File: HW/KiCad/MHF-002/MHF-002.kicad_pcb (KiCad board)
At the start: 2 copper layers, 99.9 x 99.9 mm, 264 parts, among them J1 VGA, J10 I2C, J100 x, J101 x, J102 x, J103 x, J104 x, J105 x, J106 x, J107 +3V3, J108 GND, J109 +3V3, J11 + 5V -, J110 +5V, J111 GND, J112 GND, J12 Reset, J13 +5V, J14 GND, J15 AREF, J16 XTAL2, J17 SDcard, J18 XTAL1, J19 AVCC, J2 PS/2, J20 SDcardpins, J21 x, J22 x, J23 VIN 12V, J24 AND_B1, J25 AND_B2, J26 AND_C1, J27 AND_C2, J28 AND_D1, J29 AND_D2, J3 RCA, J30 AND_Dx, J31 AND_Cx, J32 AND_Bx, J33 NOTF, J34 NOTE, J35 NOTEx, J36 NOTFx, J37 x, J38 x, J39 x, J4 SysBus, J40 x, J41 x, J42 x, J43 x, J44 x, J45 x, J46 x, J47 x, J48 x, J49 x, J5 Micro, J50 x, J51 x, J52 x, J53 x, J54 x, J55 x, J56 x, J57 x, J58 x, J59 x, J6 SysBus, J60 x, J61 x, J62 x, J63 x, J64 x, J65 x, J66 x, J67 x, J68 x, J69 x, J7 SPI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

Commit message: photos and tests
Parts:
- U14: value 5.0V -> AMS1117-5.0
- U15: value 3.3 V -> AMS1117-3.3
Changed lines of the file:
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@@
 		)
 		(property "Value" "+ 5V -"
-			(at -1.23661 -2.7672 0)
+			(at -1.23661 -2.7672 180)
 			(unlocked yes)
 			(layer "F.SilkS")
@@
 			)
 		)
-		(property "Value" "3.3 V"
+		(property "Value" "AMS1117-3.3"
 			(at 5.62716 -1.77458 270)
 			(unlocked yes)
@@
 			)
 		)
-		(property "Value" "5.0V"
+		(property "Value" "AMS1117-5.0"
 			(at 4.55012 -2.31835 90)
 			(unlocked yes)

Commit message: external memory
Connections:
- net Net-(M3-A0) renamed /L3
- net Net-(M3-A1) renamed /L2
- net Net-(M3-A2) renamed /L1
- net Net-(M3-A3) renamed /L0
- net Net-(M3-A4) renamed /L4
- net Net-(M3-A5) renamed /L5
- net Net-(M3-A6) renamed /L6
- net Net-(M3-A7) renamed /L7

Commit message: +footprints
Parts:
- removed U4: 74HC165, Package_DIP:DIP-16_W7.62mm
- added JP15: TX340, Jumper:SolderJumper-2_P1.3mm_Open_RoundedPad1.0x1.5mm, F.Cu at (-18.3, 35.7)
- added JP16: RX340, Jumper:SolderJumper-2_P1.3mm_Open_RoundedPad1.0x1.5mm, F.Cu at (-18.3, 39.2)
- added JP17: CTS340, Jumper:SolderJumper-2_P1.3mm_Open_RoundedPad1.0x1.5mm, F.Cu at (-18.3, 42.8)
- added JP18: DTR340, Jumper:SolderJumper-2_P1.3mm_Open_RoundedPad1.0x1.5mm, F.Cu at (-18.3, 46.3)
- added JP19: RTS340, Jumper:SolderJumper-2_P1.3mm_Open_RoundedPad1.0x1.5mm, F.Cu at (-18.3, 49.9)
- added JP20: USB_GND, MHF:G_rework_jumper_2.54mm, F.Cu at (94.5, 40.6)
- added M1: CP2102, MHF:G_CP2102, F.Cu at (223.5, 106.7)
- added R44: 10k, Resistor_SMD:R_0805_2012Metric_Pad1.20x1.40mm_HandSolder, F.Cu at (-3.26, 51.7)
- added R45: 10k, Resistor_SMD:R_0805_2012Metric_Pad1.20x1.40mm_HandSolder, F.Cu at (-3.26, 54.7)
- added U5: 74HC166, MHF:G_SOIC-16_3.9x9.9mm_HandSolder, F.Cu at (230.2, 16.8)
- C9: footprint Capacitor_SMD:C_0603_1608Metric_Pad1.08x0.95mm_HandSolder -> Capacitor_THT:C_Disc_D3.0mm_W2.0mm_P2.50mm
- J2: footprint other.pretty:J_Mini-DIN-6 -> MHF:J_Mini-DIN-6
- J3: footprint Gilhad:CUI_RCJ-047_Yellow -> MHF:CUI_RCJ-047_Yellow
- M3, M5: footprint Package_SO:TSOP-I-32_18.4x8mm_P0.5mm -> MHF:G_TSOP-I-32_18.4x8mm_HandSolder
- U1: footprint Package_QFP:TQFP-100_14x14mm_P0.5mm -> MHF:G_TQFP-100_14x14mm_HandSolder
- U10, U11, U12: footprint Package_SO:SOIC-20W_7.5x12.8mm_P1.27mm -> MHF:G_SOIC-20W_7.5x12.8mm_P1.27mm_HandSolder
- moved Y1 136.3 mm to (216.1, 38.5), turned to 0 degrees
- moved M5 134.4 mm to (179.2, 53.3)
- moved C13 134.2 mm to (219.5, 42.4), turned to 180 degrees
- moved R29 133.5 mm to (216.0, 42.4), turned to 180 degrees
- moved C14 132.7 mm to (212.7, 42.4), turned to 0 degrees
- moved U1 129.5 mm to (214.2, 54.2), turned to 180 degrees
- moved J1 128.3 mm to (238.9, 95.2)
- moved J3 128.2 mm to (252.3, 54.9)
- moved H5 128.1 mm to (157.4, 30.4)
- moved H6 128.0 mm to (247.4, 30.4)
- moved H8 128.0 mm to (157.4, 120.4)
- moved H7 128.0 mm to (247.4, 120.4)
- moved J2 128.0 mm to (252.1, 72.4)
- moved J4 127.3 mm to (157.5, 36.1)
- moved J6 127.2 mm to (162.6, 36.1)
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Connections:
- C9 pad 2: Net-(U13-~{DTR}) -> Net-(JP18-B)
- J5 pad 5: GND -> Net-(J5-GND)
- J5 pad 6: GND -> Net-(J5-GND)
- JP55 pad 2: PS2 Data -> Net-(JP55-B)
- JP56 pad 2: PS2 Clock -> Net-(JP56-B)
- N1 pad 2: VGA data 4 -> VSyncVGA
- PB1 pad 5: PS2-OE -> CTS
- PB1 pad 6: X16 -> RTS
- PE1 pad 3: CTS -> PS2-OE
- PE1 pad 4: RTS -> X16
- PF1 pad 1: Shared_data_D0 -> VGA data 0
- PF1 pad 2: Shared_data_D1 -> VGA data 1
- PF1 pad 3: Shared_data_D2 -> VGA data 2
- PF1 pad 4: Shared_data_D3 -> VGA data 3
- PF1 pad 5: Shared_data_D4 -> VGA data 4
- PF1 pad 6: Shared_data_D5 -> VGA data 5
- PF1 pad 7: Shared_data_D6 -> VGA data 6
- PF1 pad 8: Shared_data_D7 -> VGA data 7
- PL1 pad 1: VGA data 0 -> Shared_data_D0
- PL1 pad 2: VGA data 1 -> Shared_data_D1
- PL1 pad 3: VGA data 2 -> Shared_data_D2
- PL1 pad 4: VGA data 3 -> Shared_data_D3
- PL1 pad 5: VGA data 4 -> Shared_data_D4
- PL1 pad 6: VGA data 5 -> Shared_data_D5
- PL1 pad 7: VGA data 6 -> Shared_data_D6
- PL1 pad 8: VGA data 7 -> Shared_data_D7
- R28 pad 2: Net-(U13-~{DTR}) -> Net-(JP18-B)
- U1 pad 23: PS2-OE -> CTS
- U1 pad 24: X16 -> RTS
- U1 pad 35: VGA data 0 -> Shared_data_D0
- U1 pad 36: VGA data 1 -> Shared_data_D1
- U1 pad 37: VGA data 2 -> Shared_data_D2
- U1 pad 38: VGA data 3 -> Shared_data_D3
- U1 pad 39: VGA data 4 -> Shared_data_D4
- U1 pad 4: CTS -> PS2-OE
- U1 pad 40: VGA data 5 -> Shared_data_D5
- U1 pad 41: VGA data 6 -> Shared_data_D6
- U1 pad 42: VGA data 7 -> Shared_data_D7
- U1 pad 5: RTS -> X16
- U1 pad 90: Shared_data_D7 -> VGA data 7
- U1 pad 91: Shared_data_D6 -> VGA data 6
- U1 pad 92: Shared_data_D5 -> VGA data 5
- U1 pad 93: Shared_data_D4 -> VGA data 4
- U1 pad 94: Shared_data_D3 -> VGA data 3
- U1 pad 95: Shared_data_D2 -> VGA data 2
- U1 pad 96: Shared_data_D1 -> VGA data 1
- U1 pad 97: Shared_data_D0 -> VGA data 0
- U13 pad 13: Net-(U13-~{DTR}) -> Net-(JP18-A)
- U13 pad 14: RTS -> Net-(JP19-A)
- U13 pad 2: M8TXD -> Net-(JP15-A)
- U13 pad 3: M8RXD -> Net-(JP16-A)
- U13 pad 9: CTS -> Net-(JP17-A)
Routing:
- net Shared_data_D1: track 149.9 -> 216.1 mm
- net VGA data 1: track 66.2 -> 0.00 mm
- net VGA data 6: track 57.8 -> 0.00 mm, vias 1 -> 0
- net Shared_data_D6: track 105.7 -> 163.5 mm, vias 2 -> 3
- net VGA data 2: track 55.5 -> 0.00 mm, vias 2 -> 0
- net Shared_data_D2: track 80.8 -> 136.3 mm, vias 1 -> 3
- net VGA data 7: track 55.5 -> 0.00 mm, vias 2 -> 0
- net Shared_data_D7: track 96.0 -> 151.5 mm, vias 1 -> 3
- net Shared_data_D0: track 76.2 -> 129.0 mm, vias 0 -> 1
- net VGA data 0: track 52.8 -> 0.00 mm, vias 1 -> 0
- net Shared_data_D5: track 102.4 -> 155.1 mm
- net VGA data 5: track 52.7 -> 0.00 mm
- net Net-(U13-~{DTR}): track 5.72 -> 0.00 mm, vias 1 -> 0
- net (no net): track 0.00 -> 5.72 mm, vias 0 -> 1
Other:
- board size 99.9 x 99.9 mm -> 228 x 101.2 mm

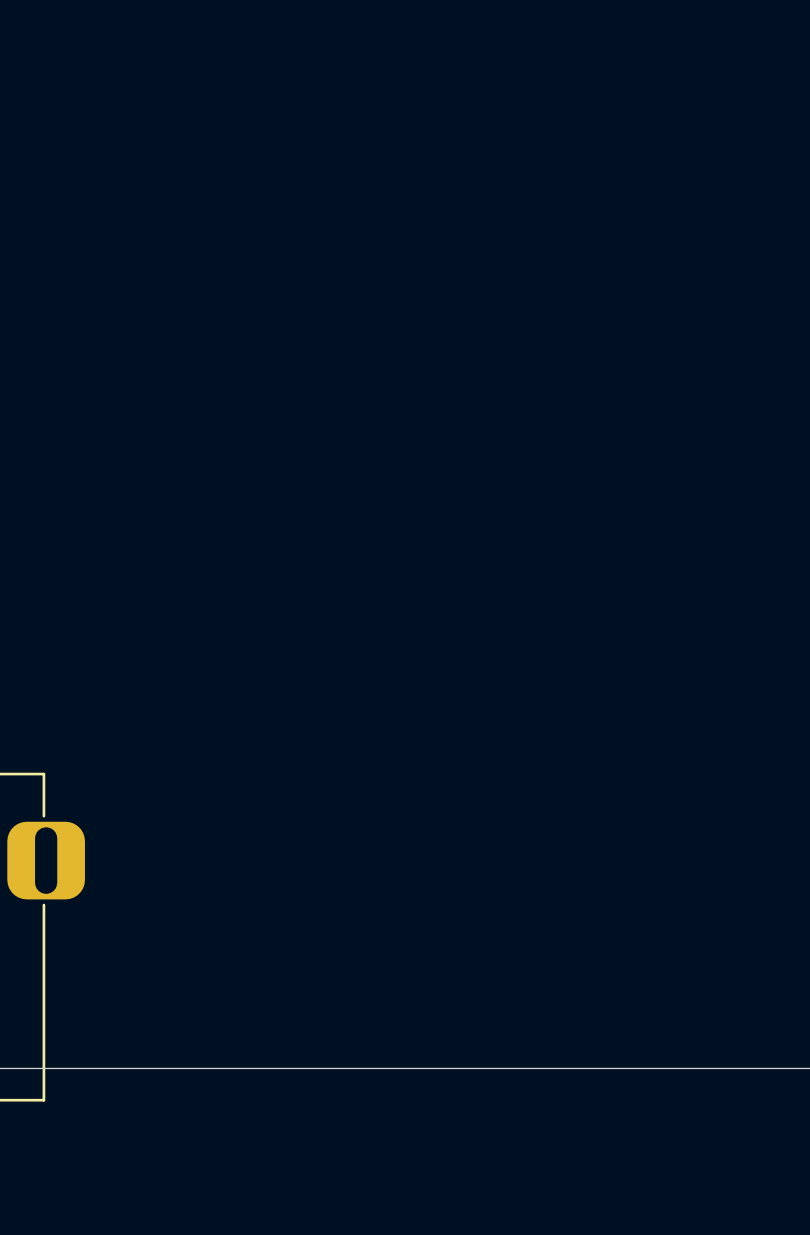
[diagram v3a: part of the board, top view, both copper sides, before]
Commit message: +cp2102 +SDCard
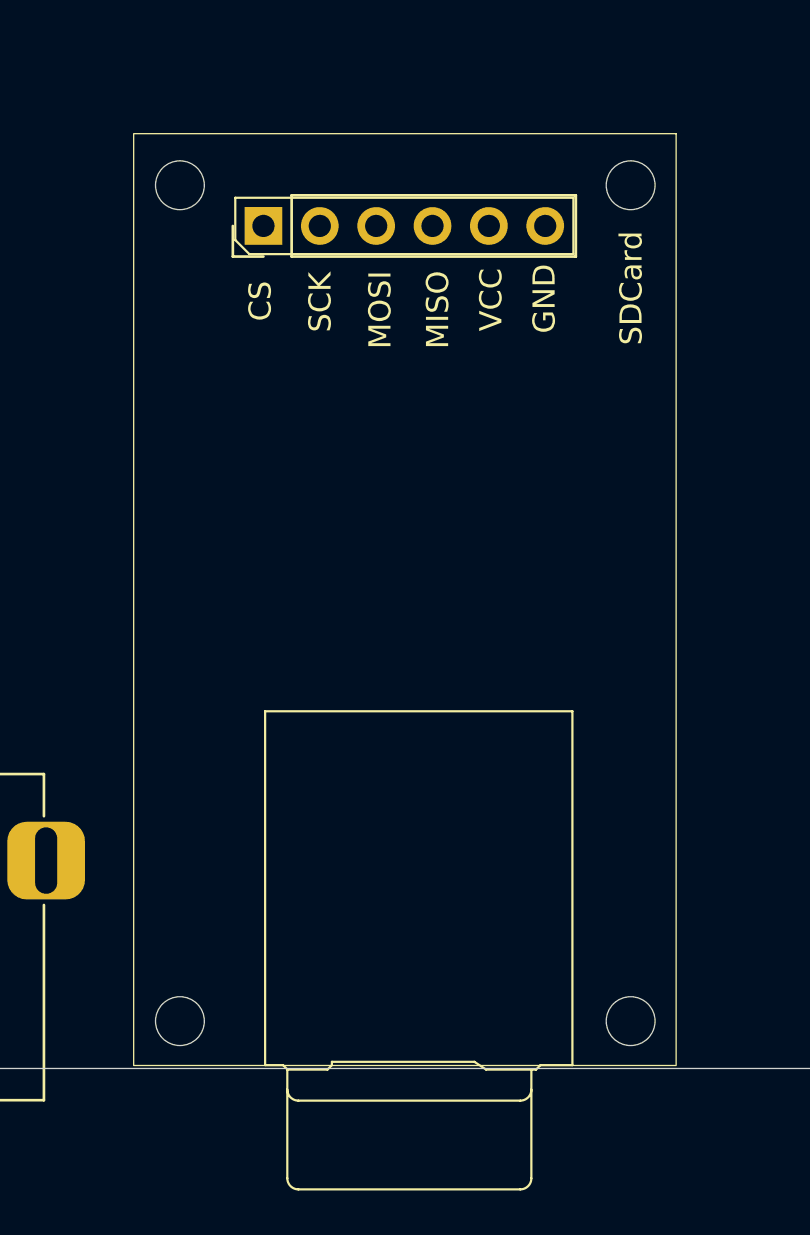
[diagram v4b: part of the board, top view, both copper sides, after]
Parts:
- added J113: SDCard, MHF:SDCard, F.Cu at (184.7, 87.4)

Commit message: more small fixes
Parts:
- removed U6: 74AHC373, Package_SO:TSSOP-20_4.4x6.5mm_P0.65mm
- added JP21: TX2102, Jumper:SolderJumper-2_P1.3mm_Open_RoundedPad1.0x1.5mm, F.Cu at (-49.6, 36.4)
- added JP22: RX2102, Jumper:SolderJumper-2_P1.3mm_Open_RoundedPad1.0x1.5mm, F.Cu at (-49.6, 39.9)
- added JP23: CTS2102, Jumper:SolderJumper-2_P1.3mm_Open_RoundedPad1.0x1.5mm, F.Cu at (-49.6, 43.5)
- added JP24: DTR2102, Jumper:SolderJumper-2_P1.3mm_Open_RoundedPad1.0x1.5mm, F.Cu at (-49.6, 47.0)
- added JP25: RTS2102, Jumper:SolderJumper-2_P1.3mm_Open_RoundedPad1.0x1.5mm, F.Cu at (-49.6, 50.6)
- added JP26: PS/2, Connector_PinHeader_2.54mm:PinHeader_1x02_P2.54mm_Vertical, F.Cu at (6.38, 1.79)
- added JP27: VGA, Connector_PinHeader_2.54mm:PinHeader_1x06_P2.54mm_Vertical, F.Cu at (1.79, 1.79)
- added JP28: RCA, Connector_PinHeader_2.54mm:PinHeader_1x02_P2.54mm_Vertical, F.Cu at (11.0, 1.79)
- added U4: 74AHC573, Package_SO:TSSOP-20_4.4x5mm_P0.5mm, F.Cu at (141.7, 11.3)
- C1: value 100 pF -> 10 nF
- Q1: value BC107 -> S8050
- R1: value 3k3/22k -> 20k
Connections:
- net Net-(JP18-B) renamed DTR
- M1 pad 3: unconnected-(M1-RTS-Pad3) -> Net-(JP25-A)
- M1 pad 4: unconnected-(M1-CTS-Pad4) -> Net-(JP23-A)
- M1 pad 5: unconnected-(M1-DTR-Pad5) -> Net-(JP24-A)
- M1 pad 6: unconnected-(M1-RXD-Pad6) -> Net-(JP22-A)
- M1 pad 7: unconnected-(M1-TXD-Pad7) -> Net-(JP21-A)
- M1 pad 8: unconnected-(M1-+5V-Pad8) -> +5V
- M1 pad 9: unconnected-(M1-GND-Pad9) -> GND
- S1 pad 1: GND -> Reset
- S1 pad 2: GND -> Reset
- S1 pad 3: Reset -> GND
- S1 pad 4: Reset -> GND
- S1 pad 5: GND -> (no net)
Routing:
- net Net-(JP18-A): track 0.00 -> 5.72 mm, vias 0 -> 1
- net (no net): track 5.72 -> 0.00 mm, vias 1 -> 0

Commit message: +Switch
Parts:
- added LED10: Reset, LED_SMD:LED_0805_2012Metric, F.Cu at (31.6, -4.69)
- added LED9: SYSTEM, LED_SMD:LED_0805_2012Metric, F.Cu at (31.6, -7.73)
- added R46: 10k, Resistor_SMD:R_0805_2012Metric_Pad1.20x1.40mm_HandSolder, F.Cu at (36.0, -8.00)
- added R47: 10k, Resistor_SMD:R_0805_2012Metric_Pad1.20x1.40mm_HandSolder, F.Cu at (36.0, -5.49)
- C12: footprint Capacitor_SMD:C_0603_1608Metric_Pad1.08x0.95mm_HandSolder -> Capacitor_THT:C_Disc_D3.0mm_W2.0mm_P2.50mm
- C13, C14: value 100n -> 22p
- JP20: footprint MHF:G_rework_jumper_2.54mm -> MHF:G_Rework_Jumper_Bridged_2.54mm
- S1: footprint Arduino Mega 2560:SW_TS06-667-30-BK-100-G-SMT-TR -> MHF:G_Arduino_switch
- moved S1 109.4 mm to (195.6, 36.4)

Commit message: fixing small problems
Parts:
- added JP30: USB_PWR, MHF:G_Rework_Jumper_Bridged_2.54mm, F.Cu at (113.7, 103.0)
- added JP31: USB_D+, MHF:G_Rework_Jumper_Bridged_2.54mm, F.Cu at (113.7, 97.9)
- added JP32: USB_D-, MHF:G_Rework_Jumper_Bridged_2.54mm, F.Cu at (113.7, 100.4)
- U3: value 74LS08 -> 74HC08
- moved U12 97.9 mm to (112.9, -1.77)
- moved U11 70.9 mm to (91.9, 0.93)
- moved U2 68.0 mm to (105.5, 168.0)
- moved JP20 58.0 mm to (113.7, 95.4), turned to 180 degrees
- moved J5 54.5 mm to (121.6, 97.1)
- moved U10 47.1 mm to (65.8, -2.80)
- moved U13 29.8 mm to (130.9, 28.8)
- moved U3 24.5 mm to (126.1, 67.3)
- moved Y2 19.1 mm to (104.2, 17.5)
- moved Q1 12.3 mm to (119.5, 59.9)
- moved C12 10.9 mm to (120.1, 42.7)
- moved Cx15 8.90 mm to (75.9, 66.3)
- moved U1 1.27 mm to (214.4, 55.4)
- moved J20 1.05 mm to (59.8, 82.9)
- moved C9 0.70 mm to (109.8, 46.9)
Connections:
- F1 pad 2: Net-(J5-VBUS) -> Net-(JP30-B)
- R24 pad 2: Net-(J5-D+) -> Net-(JP31-B)
- R25 pad 2: Net-(J5-D-) -> Net-(JP32-B)
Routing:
- net GND: track 893.0 -> 0.00 mm, vias 11 -> 0
- net +5V: track 782.4 -> 0.00 mm, vias 15 -> 0
- net Shared_data_D1: track 216.1 -> 0.00 mm
- net Shared_data_D6: track 163.5 -> 0.00 mm, vias 3 -> 0
- net Shared_data_D5: track 155.1 -> 0.00 mm, vias 2 -> 0
- net HSyncVGA: track 152.9 -> 0.00 mm, vias 2 -> 0
- net Shared_data_D7: track 151.5 -> 0.00 mm, vias 3 -> 0
- net VGA Latch: track 143.0 -> 0.00 mm, vias 2 -> 0
- net Shared_data_D2: track 136.3 -> 0.00 mm, vias 3 -> 0
- net Shared_data_D0: track 129.0 -> 0.00 mm, vias 1 -> 0
- net X16: track 126.0 -> 0.00 mm, vias 2 -> 0
- net SIGNAL_RCA: track 125.7 -> 0.00 mm, vias 2 -> 0
- net PS2-OE: track 120.8 -> 0.00 mm, vias 1 -> 0
- net Shared_Address_A10: track 120.6 -> 0.00 mm, vias 2 -> 0
- net Reset: track 116.0 -> 0.00 mm, vias 5 -> 0
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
